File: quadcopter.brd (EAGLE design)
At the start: 138.5 x 138.5 mm, 66 parts, among them J1 AVR_SPI_PRG_6NS, Q1 N-CHANNEL_MOSFET, Q2 N-CHANNEL_MOSFET, Q3 N-CHANNEL_MOSFET, Q4 N-CHANNEL_MOSFET, SW2 PUSHBUTTON_SMD-VERTICAL-1, U1 ATMEGA128RFA1

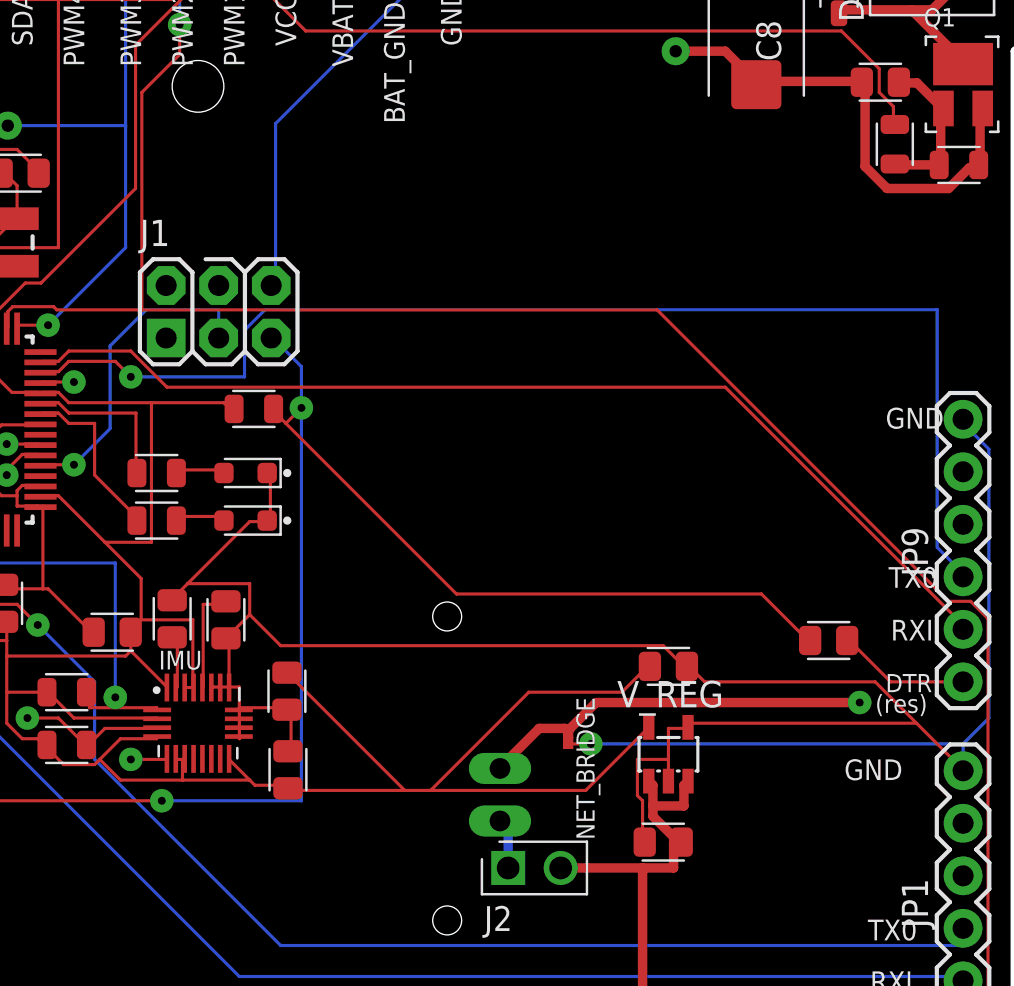
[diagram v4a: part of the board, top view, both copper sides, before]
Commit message: Fix gnd/bat_gnd issue and re ran cam job
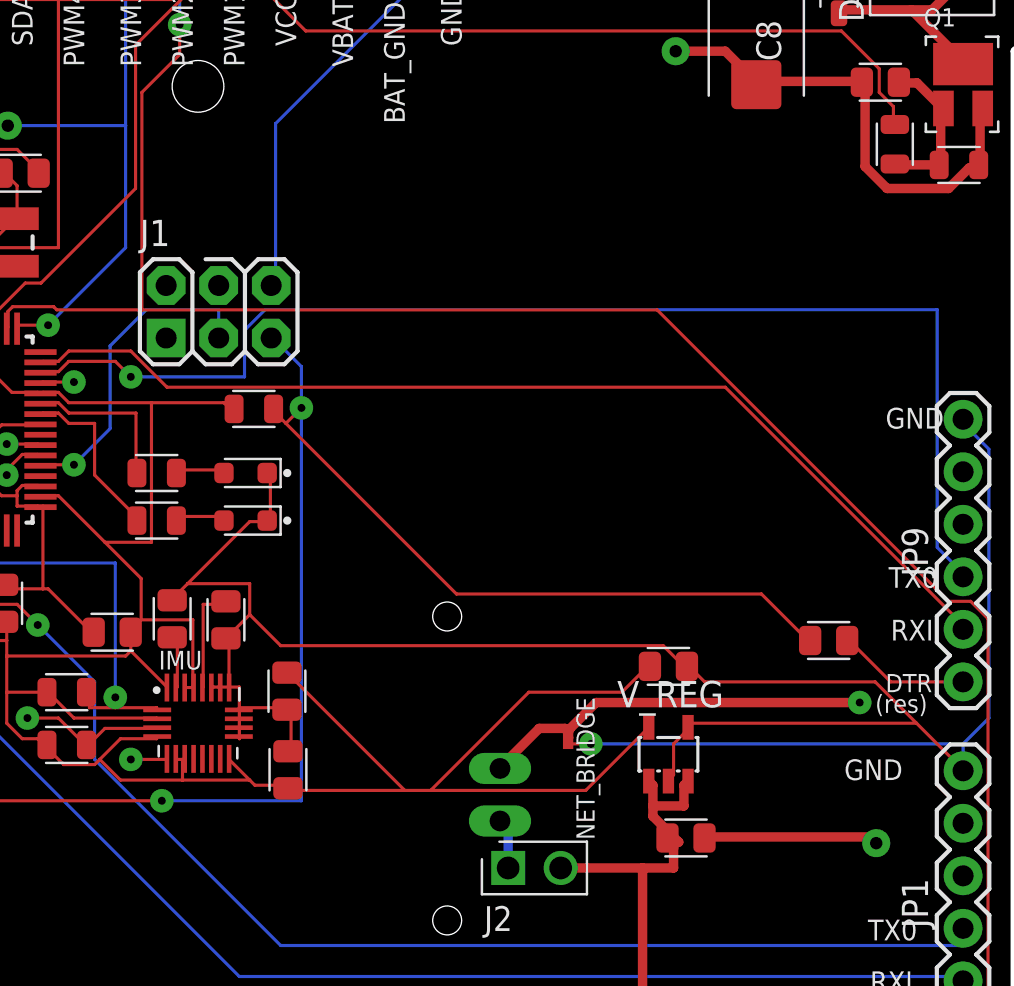
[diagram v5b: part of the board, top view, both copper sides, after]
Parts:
- moved C23 1.12 mm to (93.6, 64.5), turned to 180 degrees
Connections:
- net BAT_GND: now also C23.1
- net GND: no longer C23.1
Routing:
- net BAT_GND: track 122.8 -> 131.3 mm, vias 6 -> 7
- net GND: track 244.0 -> 237.7 mm
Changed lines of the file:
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@@
 <attribute name="MPN" value="GRM21BR71H104KA01L" x="65.85" y="74.4" size="1.778" layer="27" rot="R180" display="off"/>
 </element>
-<element name="C23" library="quadparts_prebuilt" package="CAPC2012X140_HS" value="1uF" x="92.5" y="64.25">
-<attribute name="DIST" value="Digikey" x="92.5" y="64.25" size="1.778" layer="27" display="off"/>
-<attribute name="DISTPN" value="490-4736-1-ND" x="92.5" y="64.25" size="1.778" layer="27" display="off"/>
-<attribute name="MFR" value="Murata Electronics North America" x="92.5" y="64.25" size="1.778" layer="27" display="off"/>
-<attribute name="MPN" value="GRM21BR71H105KA12L" x="92.5" y="64.25" size="1.778" layer="27" display="off"/>
+<element name="C23" library="quadparts_prebuilt" package="CAPC2012X140_HS" value="1uF" x="93.6" y="64.45" rot="R180">
+<attribute name="DIST" value="Digikey" x="93.6" y="64.45" size="1.778" layer="27" rot="R180" display="off"/>
+<attribute name="DISTPN" value="490-4736-1-ND" x="93.6" y="64.45" size="1.778" layer="27" rot="R180" display="off"/>
+<attribute name="MFR" value="Murata Electronics North America" x="93.6" y="64.45" size="1.778" layer="27" rot="R180" display="off"/>
+<attribute name="MPN" value="GRM21BR71H105KA12L" x="93.6" y="64.45" size="1.778" layer="27" rot="R180" display="off"/>
 </element>
 <element name="C24" library="quadparts_prebuilt" package="CAPC2012X140_HS" value="1uF" x="92.75" y="72.75">
@@
 <contactref element="V_REG" pad="2"/>
 <contactref element="V_REG" pad="4"/>
-<contactref element="C23" pad="1"/>
 <contactref element="C24" pad="2"/>
 <contactref element="J3" pad="10"/>
@@
 <wire x1="69.5" y1="76.75" x2="72.5" y2="76.75" width="0.1524" layer="1"/>
 <wire x1="71.5" y1="74.25" x2="71.35" y2="74.105" width="0.1524" layer="1"/>
-<wire x1="92.75" y1="69.75" x2="92.75" y2="68.25" width="0.1524" layer="1"/>
-<wire x1="92.75" y1="68.25" x2="92.75" y2="67.2" width="0.1524" layer="1"/>
-<wire x1="93.5" y1="69.75" x2="92.75" y2="69.75" width="0.1524" layer="1"/>
-<wire x1="93.5" y1="69.75" x2="93.7" y2="69.8" width="0.1524" layer="1"/>
-<wire x1="91.5" y1="66.25" x2="91.5" y2="64.25" width="0.1524" layer="1"/>
-<wire x1="91.25" y1="66.5" x2="91.5" y2="66.25" width="0.1524" layer="1"/>
-<wire x1="91.25" y1="68.25" x2="91.25" y2="66.5" width="0.1524" layer="1"/>
-<wire x1="92.75" y1="68.25" x2="91.25" y2="68.25" width="0.1524" layer="1"/>
-<wire x1="91.5" y1="64.25" x2="91.605" y2="64.25" width="0.1524" layer="1"/>
 <wire x1="54.75" y1="77" x2="53.75" y2="77" width="0.1524" layer="1"/>
 <wire x1="53.75" y1="77" x2="53" y2="77" width="0.1524" layer="1"/>
@@
 <via x="53" y="93.5" extent="1-16" drill="0.381"/>
 <via x="50.75" y="93.5" extent="1-16" drill="0.381"/>
+<wire x1="93" y1="69" x2="93" y2="67.5" width="0.1524" layer="1"/>
+<wire x1="93.5" y1="69.5" x2="93" y2="69" width="0.1524" layer="1"/>
+<wire x1="93" y1="67.5" x2="92.75" y2="67.2" width="0.1524" layer="1"/>
+<wire x1="93.5" y1="69.5" x2="93.7" y2="69.8" width="0.1524" layer="1"/>
 </signal>
 <signal name="N$2">
@@
 <wire x1="66.5" y1="93" x2="62.75" y2="89.25" width="0.1524" layer="16"/>
 <wire x1="66.5" y1="98.9" x2="66.5" y2="107" width="0.1524" layer="16"/>
-<wire x1="66.5" y1="98.8" x2="66.5" y2="93" width="0.1524" layer="16"/>
+<wire x1="66.5" y1="98.9" x2="66.5" y2="93" width="0.1524" layer="16"/>
 <wire x1="61.25" y1="89.25" x2="61.25" y2="89.081" width="0.1524" layer="1"/>
 <wire x1="66.5" y1="107" x2="66.62" y2="107" width="0.1524" layer="16"/>
@@
 <via x="60.8" y="98.9" extent="1-16" drill="0.6"/>
 <wire x1="60.8" y1="98.9" x2="66.5" y2="98.9" width="0.1524" layer="16"/>
-<wire x1="66.5" y1="98.9" x2="66.5" y2="98.8" width="0.1524" layer="16"/>
 <via x="53.7" y="98.9" extent="1-16" drill="0.6"/>
 <wire x1="60.8" y1="98.9" x2="53.7" y2="98.9" width="0.1524" layer="1"/>
@@
 <wire x1="37.5" y1="100" x2="37.895" y2="100" width="0.4572" layer="1"/>
 <wire x1="37.5" y1="100" x2="37.4904" y2="99.822" width="0.4572" layer="1"/>
+<contactref element="C23" pad="1"/>
+<via x="102.8" y="64.2" extent="1-16" drill="0.6"/>
+<wire x1="102.5" y1="64.5" x2="94.5" y2="64.5" width="0.4572" layer="1"/>
+<wire x1="94.5" y1="64.5" x2="94.495" y2="64.45" width="0.4572" layer="1"/>
+<wire x1="102.5" y1="64.5" x2="102.8" y2="64.2" width="0.4572" layer="1"/>
 </signal>
 <signal name="VBAT" class="2">
@@
 <wire x1="93.25" y1="64.25" x2="92" y2="65.5" width="0.4572" layer="1"/>
 <wire x1="92" y1="67" x2="91.8" y2="67.2" width="0.4572" layer="1"/>
-<wire x1="93.25" y1="64.25" x2="93.395" y2="64.25" width="0.4572" layer="1"/>
+<wire x1="93.25" y1="64.25" x2="92.705" y2="64.45" width="0.4572" layer="1"/>
 <wire x1="93.5" y1="66" x2="93.5" y2="67" width="0.4572" layer="1"/>
 <wire x1="92" y1="66" x2="93.5" y2="66" width="0.4572" layer="1"/>
@@
 <wire x1="87.54" y1="63" x2="91.5" y2="63" width="0.4572" layer="1"/>
 <wire x1="91.5" y1="63" x2="93" y2="63" width="0.4572" layer="1"/>
-<wire x1="93" y1="64.25" x2="93.395" y2="64.25" width="0.4572" layer="1"/>
+<wire x1="93" y1="64.25" x2="92.705" y2="64.45" width="0.4572" layer="1"/>
 <wire x1="102.5" y1="106" x2="101" y2="107.5" width="0.4572" layer="1"/>
 <wire x1="104" y1="106" x2="102.5" y2="106" width="0.4572" layer="1"/>
